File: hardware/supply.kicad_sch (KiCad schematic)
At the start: 14 parts

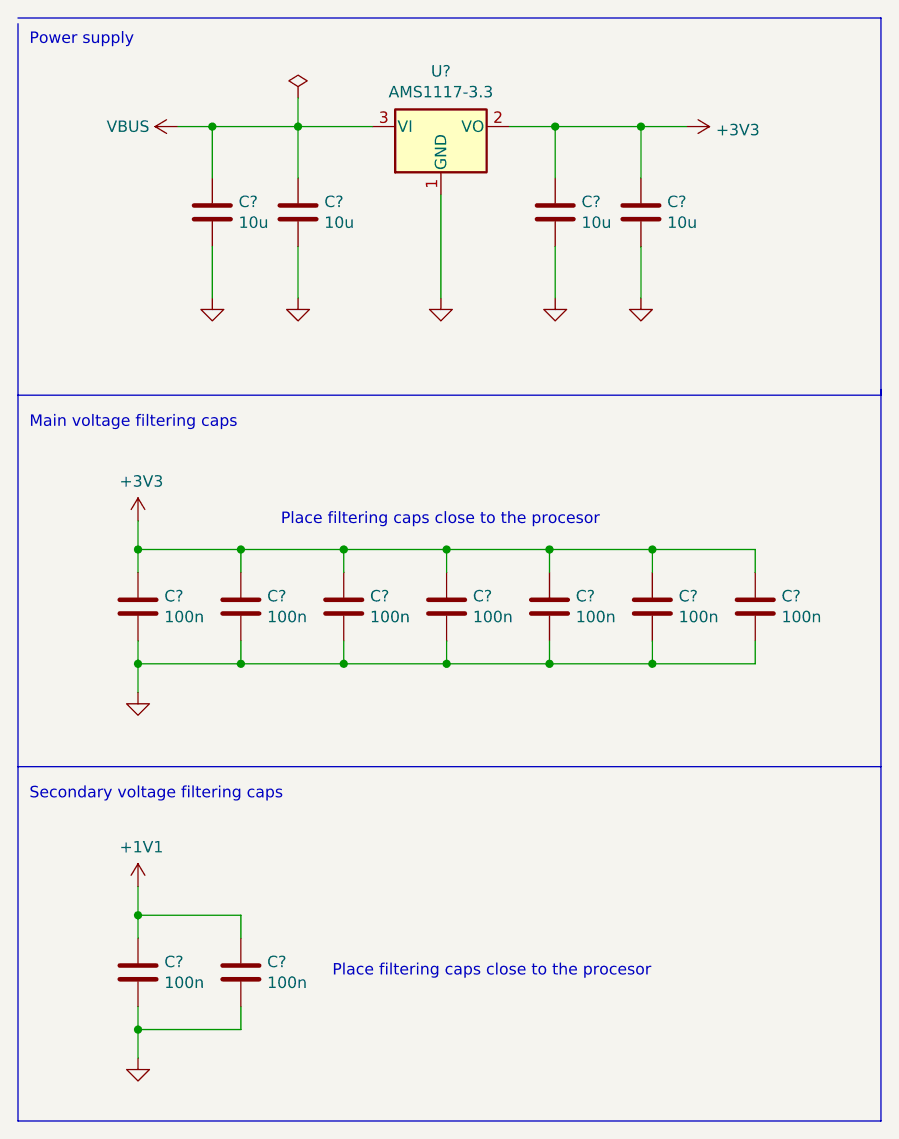
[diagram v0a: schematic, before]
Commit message: hw: Add annotations to all components
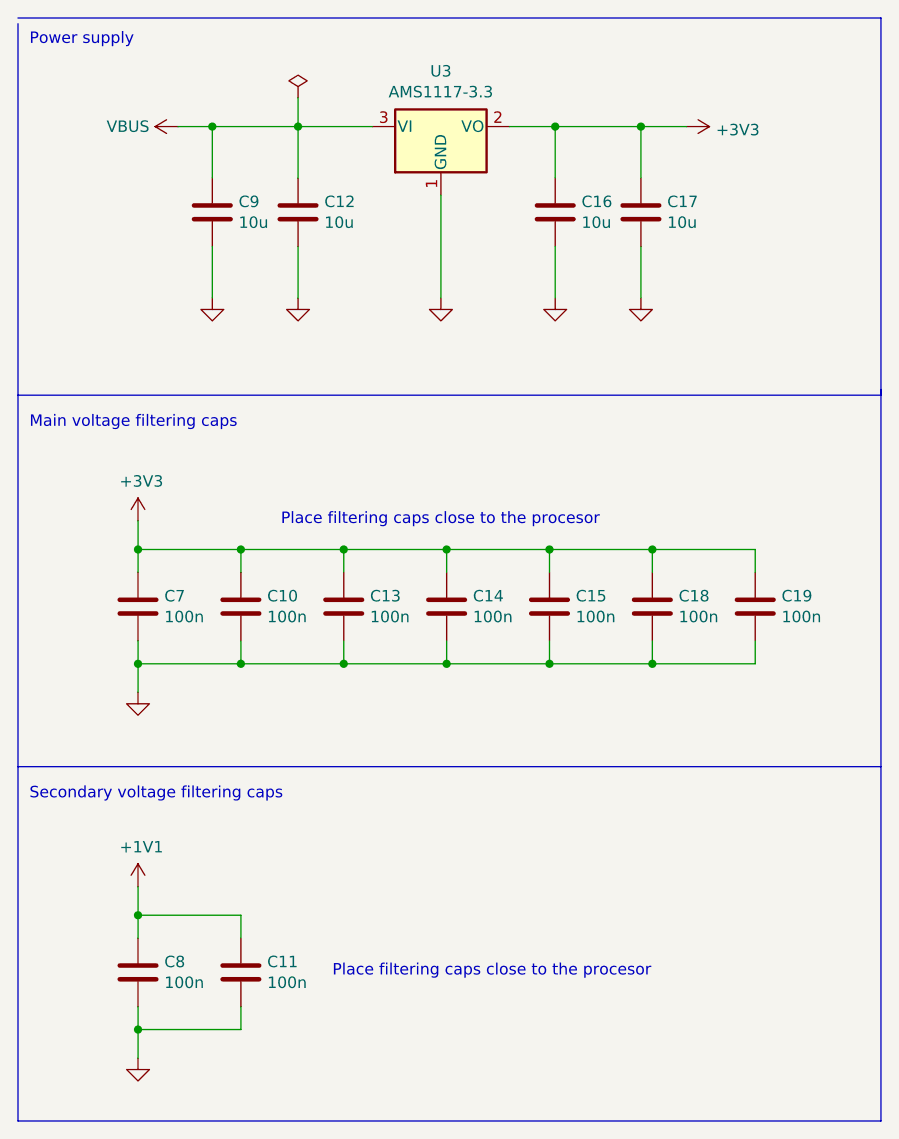
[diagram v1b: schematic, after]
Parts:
- gave numbers to parts that had none: 14
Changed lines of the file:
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@@
   (symbol (lib_id "Regulator_Linear:AMS1117-3.3") (at 144.145 39.37 0) (unit 1)
     (in_bom yes) (on_board yes)
-    (property "Reference" "U?" (id 0) (at 144.145 33.2232 0))
+    (property "Reference" "U3" (id 0) (at 144.145 33.2232 0))
     (property "Value" "AMS1117-3.3" (id 1) (at 144.145 35.5346 0))
     (property "Footprint" "Package_TO_SOT_SMD:SOT-223-3_TabPin2" (id 2) (at 144.145 34.29 0)
@@
   (symbol (lib_id "Device:C") (at 118.745 48.895 0) (unit 1)
     (in_bom yes) (on_board yes)
-    (property "Reference" "C?" (id 0) (at 121.666 47.7266 0)
+    (property "Reference" "C9" (id 0) (at 121.666 47.7266 0)
       (effects (font (size 1.27 1.27)) (justify left))
     )
@@
   (symbol (lib_id "Device:C") (at 110.49 92.71 0) (unit 1)
     (in_bom yes) (on_board yes)
-    (property "Reference" "C?" (id 0) (at 113.411 91.5416 0)
+    (property "Reference" "C7" (id 0) (at 113.411 91.5416 0)
       (effects (font (size 1.27 1.27)) (justify left))
     )
@@
   (symbol (lib_id "power:GND") (at 156.845 58.42 0) (unit 1)
     (in_bom yes) (on_board yes)
-    (property "Reference" "#PWR?" (id 0) (at 156.845 64.77 0)
+    (property "Reference" "#PWR022" (id 0) (at 156.845 64.77 0)
       (effects (font (size 1.27 1.27)) hide)
     )
@@
   (symbol (lib_id "power:GND") (at 166.37 58.42 0) (unit 1)
     (in_bom yes) (on_board yes)
-    (property "Reference" "#PWR?" (id 0) (at 166.37 64.77 0)
+    (property "Reference" "#PWR023" (id 0) (at 166.37 64.77 0)
       (effects (font (size 1.27 1.27)) hide)
     )
@@
   (symbol (lib_id "Device:C") (at 110.49 133.35 0) (unit 1)
     (in_bom yes) (on_board yes)
-    (property "Reference" "C?" (id 0) (at 113.411 132.1816 0)
+    (property "Reference" "C8" (id 0) (at 113.411 132.1816 0)
       (effects (font (size 1.27 1.27)) (justify left))
     )
@@
   (symbol (lib_id "Device:C") (at 133.35 92.71 0) (unit 1)
     (in_bom yes) (on_board yes)
-    (property "Reference" "C?" (id 0) (at 136.271 91.5416 0)
+    (property "Reference" "C13" (id 0) (at 136.271 91.5416 0)
       (effects (font (size 1.27 1.27)) (justify left))
     )
@@
   (symbol (lib_id "Device:C") (at 156.21 92.71 0) (unit 1)
     (in_bom yes) (on_board yes)
-    (property "Reference" "C?" (id 0) (at 159.131 91.5416 0)
+    (property "Reference" "C15" (id 0) (at 159.131 91.5416 0)
       (effects (font (size 1.27 1.27)) (justify left))
     )
@@
   (symbol (lib_id "Device:C") (at 179.07 92.71 0) (unit 1)
     (in_bom yes) (on_board yes)
-    (property "Reference" "C?" (id 0) (at 181.991 91.5416 0)
+    (property "Reference" "C19" (id 0) (at 181.991 91.5416 0)
       (effects (font (size 1.27 1.27)) (justify left))
     )
@@
   (symbol (lib_id "power:VBUS") (at 114.935 39.37 90) (unit 1)
     (in_bom yes) (on_board yes)
-    (property "Reference" "#PWR?" (id 0) (at 118.745 39.37 0)
+    (property "Reference" "#PWR018" (id 0) (at 118.745 39.37 0)
       (effects (font (size 1.27 1.27)) hide)
     )
@@
   (symbol (lib_id "power:PWR_FLAG") (at 128.27 36.195 0) (unit 1)
     (in_bom yes) (on_board yes)
-    (property "Reference" "#FLG?" (id 0) (at 128.27 34.29 0)
+    (property "Reference" "#FLG01" (id 0) (at 128.27 34.29 0)
       (effects (font (size 1.27 1.27)) hide)
     )
@@
   (symbol (lib_id "power:GND") (at 110.49 142.875 0) (unit 1)
     (in_bom yes) (on_board yes)
-    (property "Reference" "#PWR?" (id 0) (at 110.49 149.225 0)
+    (property "Reference" "#PWR017" (id 0) (at 110.49 149.225 0)
       (effects (font (size 1.27 1.27)) hide)
     )
@@
   (symbol (lib_id "power:GND") (at 118.745 58.42 0) (unit 1)
     (in_bom yes) (on_board yes)
-    (property "Reference" "#PWR?" (id 0) (at 118.745 64.77 0)
+    (property "Reference" "#PWR019" (id 0) (at 118.745 64.77 0)
       (effects (font (size 1.27 1.27)) hide)
     )
@@
   (symbol (lib_id "power:GND") (at 128.27 58.42 0) (unit 1)
     (in_bom yes) (on_board yes)
-    (property "Reference" "#PWR?" (id 0) (at 128.27 64.77 0)
+    (property "Reference" "#PWR020" (id 0) (at 128.27 64.77 0)
       (effects (font (size 1.27 1.27)) hide)
     )
@@
   (symbol (lib_id "power:+3V3") (at 171.45 39.37 270) (unit 1)
     (in_bom yes) (on_board yes)
-    (property "Reference" "#PWR?" (id 0) (at 167.64 39.37 0)
+    (property "Reference" "#PWR024" (id 0) (at 167.64 39.37 0)
       (effects (font (size 1.27 1.27)) hide)
     )
@@
   (symbol (lib_id "power:GND") (at 144.145 58.42 0) (unit 1)
     (in_bom yes) (on_board yes)
-    (property "Reference" "#PWR?" (id 0) (at 144.145 64.77 0)
+    (property "Reference" "#PWR021" (id 0) (at 144.145 64.77 0)
       (effects (font (size 1.27 1.27)) hide)
     )
@@
   (symbol (lib_id "power:+1V1") (at 110.49 123.825 0) (unit 1)
     (in_bom yes) (on_board yes)
-    (property "Reference" "#PWR?" (id 0) (at 110.49 127.635 0)
+    (property "Reference" "#PWR016" (id 0) (at 110.49 127.635 0)
       (effects (font (size 1.27 1.27)) hide)
     )
@@
   (symbol (lib_id "Device:C") (at 121.92 92.71 0) (unit 1)
     (in_bom yes) (on_board yes)
-    (property "Reference" "C?" (id 0) (at 124.841 91.5416 0)
+    (property "Reference" "C10" (id 0) (at 124.841 91.5416 0)
       (effects (font (size 1.27 1.27)) (justify left))
     )
@@
   (symbol (lib_id "Device:C") (at 156.845 48.895 0) (unit 1)
     (in_bom yes) (on_board yes)
-    (property "Reference" "C?" (id 0) (at 159.766 47.7266 0)
+    (property "Reference" "C16" (id 0) (at 159.766 47.7266 0)
       (effects (font (size 1.27 1.27)) (justify left))
     )
@@
   (symbol (lib_id "Device:C") (at 121.92 133.35 0) (unit 1)
     (in_bom yes) (on_board yes)
-    (property "Reference" "C?" (id 0) (at 124.841 132.1816 0)
+    (property "Reference" "C11" (id 0) (at 124.841 132.1816 0)
       (effects (font (size 1.27 1.27)) (justify left))
     )
@@
   (symbol (lib_id "Device:C") (at 166.37 48.895 0) (unit 1)
     (in_bom yes) (on_board yes)
-    (property "Reference" "C?" (id 0) (at 169.291 47.7266 0)
+    (property "Reference" "C17" (id 0) (at 169.291 47.7266 0)
       (effects (font (size 1.27 1.27)) (justify left))
     )
@@
   (symbol (lib_id "Device:C") (at 128.27 48.895 0) (unit 1)
     (in_bom yes) (on_board yes)
-    (property "Reference" "C?" (id 0) (at 131.191 47.7266 0)
+    (property "Reference" "C12" (id 0) (at 131.191 47.7266 0)
       (effects (font (size 1.27 1.27)) (justify left))
     )
@@
   (symbol (lib_id "power:+3V3") (at 110.49 83.185 0) (unit 1)
     (in_bom yes) (on_board yes)
-    (property "Reference" "#PWR?" (id 0) (at 110.49 86.995 0)
+    (property "Reference" "#PWR014" (id 0) (at 110.49 86.995 0)
       (effects (font (size 1.27 1.27)) hide)
     )
@@
   (symbol (lib_id "power:GND") (at 110.49 102.235 0) (unit 1)
     (in_bom yes) (on_board yes)
-    (property "Reference" "#PWR?" (id 0) (at 110.49 108.585 0)
+    (property "Reference" "#PWR015" (id 0) (at 110.49 108.585 0)
       (effects (font (size 1.27 1.27)) hide)
     )
@@
   (symbol (lib_id "Device:C") (at 144.78 92.71 0) (unit 1)
     (in_bom yes) (on_board yes)
-    (property "Reference" "C?" (id 0) (at 147.701 91.5416 0)
+    (property "Reference" "C14" (id 0) (at 147.701 91.5416 0)
       (effects (font (size 1.27 1.27)) (justify left))
     )
@@
   (symbol (lib_id "Device:C") (at 167.64 92.71 0) (unit 1)
     (in_bom yes) (on_board yes)
-    (property "Reference" "C?" (id 0) (at 170.561 91.5416 0)
-      (effects (font (size 1.27 1.27)) (justify left))
-    )
+    (property "Reference" "C18" (id 0) (at 170.561 91.5416 0)
+      (effects (font (size 1.27 1.27)) (justify left))
+    )
